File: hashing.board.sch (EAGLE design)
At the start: 136 parts, among them U1 ASIC-1, U10 EPM570GT100C5N, U2 ASIC-1, U3 ASIC-1, U4 ASIC-1, U5 ASIC-1, U6 ASIC-1, U7 ASIC-1, U8 ASIC-1, U9 AT32UC3A1256-AUT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

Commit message: before the custom cap things
before crazy edit
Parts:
- added CA1, CA2, CA3, CA4, CA5, CA6, CA7, CA8: BFL-BGA-144-SPC, casey's_custom_stuff:BFL-BGA-144-SPC
- C1, C2, C3, C4: device rcl:C-EUC0402 -> CAPACITORS:0306-REVERSE-GEO
- C5: device rcl:C-EUC0603 -> CAPACITORS:0306-REVERSE-GEO
- C6: device rcl:C-EUC0603 -> rcl:C-EUC0805
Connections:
- net GND: now also CA1.2, CA2.2, CA3.2, CA4.2, CA5.2, CA6.2, CA7.2, CA8.2
- net VDD-1VA: now also CA1.1, CA2.1, CA3.1, CA4.1
- net VDD-1VB: now also CA5.1, CA6.1, CA7.1, CA8.1

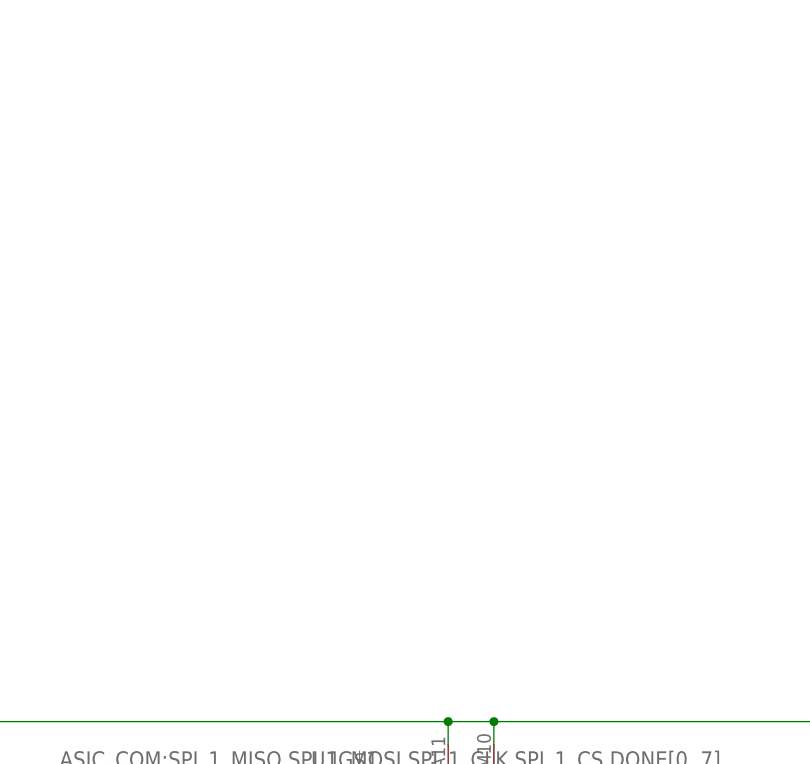
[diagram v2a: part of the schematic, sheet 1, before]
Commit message: new custom bga pkg layout
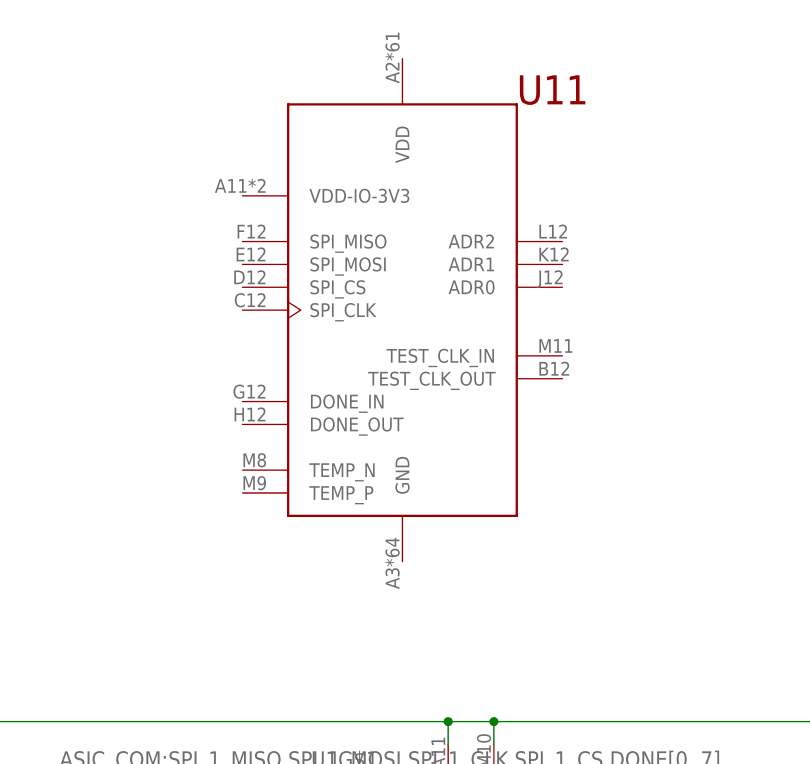
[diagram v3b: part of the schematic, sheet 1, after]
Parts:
- added U11: BFL-ASIC-1, BFL.new:BFL-ASIC-1
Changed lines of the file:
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@@
 <grid distance="0.1" unitdist="inch" unit="inch" style="lines" multiple="1" display="no" altdistance="0.01" altunitdist="inch" altunit="inch"/>
 <layers>
-<layer number="1" name="Top" color="4" fill="1" visible="yes" active="no"/>
-<layer number="2" name="Route2" color="1" fill="3" visible="yes" active="no"/>
-<layer number="3" name="Route3" color="4" fill="3" visible="yes" active="no"/>
-<layer number="14" name="Route14" color="1" fill="6" visible="yes" active="no"/>
-<layer number="15" name="Route15" color="4" fill="6" visible="yes" active="no"/>
-<layer number="16" name="Bottom" color="1" fill="1" visible="yes" active="no"/>
-<layer number="17" name="Pads" color="2" fill="1" visible="yes" active="no"/>
-<layer number="18" name="Vias" color="2" fill="1" visible="yes" active="no"/>
-<layer number="19" name="Unrouted" color="6" fill="1" visible="yes" active="no"/>
-<layer number="20" name="Dimension" color="15" fill="1" visible="yes" active="no"/>
-<layer number="21" name="tPlace" color="7" fill="1" visible="yes" active="no"/>
-<layer number="22" name="bPlace" color="7" fill="1" visible="yes" active="no"/>
-<layer number="23" name="tOrigins" color="15" fill="1" visible="yes" active="no"/>
-<layer number="24" name="bOrigins" color="15" fill="1" visible="yes" active="no"/>
-<layer number="25" name="tNames" color="7" fill="1" visible="yes" active="no"/>
-<layer number="26" name="bNames" color="7" fill="1" visible="yes" active="no"/>
-<layer number="27" name="tValues" color="7" fill="1" visible="yes" active="no"/>
-<layer number="28" name="bValues" color="7" fill="1" visible="yes" active="no"/>
+<layer number="1" name="Top" color="4" fill="1" visible="no" active="no"/>
+<layer number="2" name="Route2" color="1" fill="3" visible="no" active="no"/>
+<layer number="3" name="Route3" color="4" fill="3" visible="no" active="no"/>
+<layer number="14" name="Route14" color="1" fill="6" visible="no" active="no"/>
+<layer number="15" name="Route15" color="4" fill="6" visible="no" active="no"/>
+<layer number="16" name="Bottom" color="1" fill="1" visible="no" active="no"/>
+<layer number="17" name="Pads" color="2" fill="1" visible="no" active="no"/>
+<layer number="18" name="Vias" color="2" fill="1" visible="no" active="no"/>
+<layer number="19" name="Unrouted" color="6" fill="1" visible="no" active="no"/>
+<layer number="20" name="Dimension" color="15" fill="1" visible="no" active="no"/>
+<layer number="21" name="tPlace" color="7" fill="1" visible="no" active="no"/>
+<layer number="22" name="bPlace" color="7" fill="1" visible="no" active="no"/>
+<layer number="23" name="tOrigins" color="15" fill="1" visible="no" active="no"/>
+<layer number="24" name="bOrigins" color="15" fill="1" visible="no" active="no"/>
+<layer number="25" name="tNames" color="7" fill="1" visible="no" active="no"/>
+<layer number="26" name="bNames" color="7" fill="1" visible="no" active="no"/>
+<layer number="27" name="tValues" color="7" fill="1" visible="no" active="no"/>
+<layer number="28" name="bValues" color="7" fill="1" visible="no" active="no"/>
 <layer number="29" name="tStop" color="7" fill="3" visible="no" active="no"/>
 <layer number="30" name="bStop" color="7" fill="6" visible="no" active="no"/>
@@
 <layer number="35" name="tGlue" color="7" fill="4" visible="no" active="no"/>
 <layer number="36" name="bGlue" color="7" fill="5" visible="no" active="no"/>
-<layer number="37" name="tTest" color="7" fill="1" visible="yes" active="no"/>
-<layer number="38" name="bTest" color="7" fill="1" visible="yes" active="no"/>
+<layer number="37" name="tTest" color="7" fill="1" visible="no" active="no"/>
+<layer number="38" name="bTest" color="7" fill="1" visible="no" active="no"/>
 <layer number="39" name="tKeepout" color="4" fill="11" visible="no" active="no"/>
 <layer number="40" name="bKeepout" color="1" fill="11" visible="no" active="no"/>
@@
 <layer number="44" name="Drills" color="7" fill="1" visible="no" active="no"/>
 <layer number="45" name="Holes" color="7" fill="1" visible="no" active="no"/>
-<layer number="46" name="Milling" color="3" fill="1" visible="yes" active="no"/>
-<layer number="47" name="Measures" color="7" fill="1" visible="yes" active="no"/>
-<layer number="48" name="Document" color="7" fill="1" visible="yes" active="no"/>
-<layer number="49" name="Reference" color="7" fill="1" visible="yes" active="no"/>
-<layer number="51" name="tDocu" color="7" fill="1" visible="yes" active="no"/>
-<layer number="52" name="bDocu" color="7" fill="1" visible="yes" active="no"/>
+<layer number="46" name="Milling" color="3" fill="1" visible="no" active="no"/>
+<layer number="47" name="Measures" color="7" fill="1" visible="no" active="no"/>
+<layer number="48" name="Document" color="7" fill="1" visible="no" active="no"/>
+<layer number="49" name="Reference" color="7" fill="1" visible="no" active="no"/>
+<layer number="51" name="tDocu" color="7" fill="1" visible="no" active="no"/>
+<layer number="52" name="bDocu" color="7" fill="1" visible="no" active="no"/>
 <layer number="91" name="Nets" color="2" fill="1" visible="yes" active="yes"/>
 <layer number="92" name="Busses" color="1" fill="1" visible="yes" active="yes"/>
@@
 <part name="CA7" library="casey's_custom_stuff" deviceset="BFL-BGA-144-SPC" device=""/>
 <part name="CA8" library="casey's_custom_stuff" deviceset="BFL-BGA-144-SPC" device=""/>
+<part name="U11" library="BFL.new" deviceset="BFL-ASIC-1" device=""/>
 </parts>
 <sheets>
@@
 <instance part="FRAME2" gate="G$1" x="0" y="0"/>
 <instance part="FRAME2" gate="G$2" x="325.12" y="0"/>
+<instance part="U11" gate="G$1" x="139.7" y="213.36"/>
 </instances>
 <busses>

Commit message: broken
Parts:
- removed U11: BFL-ASIC-1, BFL.new:BFL-ASIC-1
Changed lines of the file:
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@@
 <grid distance="0.1" unitdist="inch" unit="inch" style="lines" multiple="1" display="no" altdistance="0.01" altunitdist="inch" altunit="inch"/>
 <layers>
-<layer number="1" name="Top" color="4" fill="1" visible="no" active="no"/>
-<layer number="2" name="Route2" color="1" fill="3" visible="no" active="no"/>
-<layer number="3" name="Route3" color="4" fill="3" visible="no" active="no"/>
-<layer number="14" name="Route14" color="1" fill="6" visible="no" active="no"/>
-<layer number="15" name="Route15" color="4" fill="6" visible="no" active="no"/>
-<layer number="16" name="Bottom" color="1" fill="1" visible="no" active="no"/>
-<layer number="17" name="Pads" color="2" fill="1" visible="no" active="no"/>
-<layer number="18" name="Vias" color="2" fill="1" visible="no" active="no"/>
-<layer number="19" name="Unrouted" color="6" fill="1" visible="no" active="no"/>
-<layer number="20" name="Dimension" color="15" fill="1" visible="no" active="no"/>
-<layer number="21" name="tPlace" color="7" fill="1" visible="no" active="no"/>
-<layer number="22" name="bPlace" color="7" fill="1" visible="no" active="no"/>
-<layer number="23" name="tOrigins" color="15" fill="1" visible="no" active="no"/>
-<layer number="24" name="bOrigins" color="15" fill="1" visible="no" active="no"/>
-<layer number="25" name="tNames" color="7" fill="1" visible="no" active="no"/>
-<layer number="26" name="bNames" color="7" fill="1" visible="no" active="no"/>
-<layer number="27" name="tValues" color="7" fill="1" visible="no" active="no"/>
-<layer number="28" name="bValues" color="7" fill="1" visible="no" active="no"/>
+<layer number="1" name="Top" color="4" fill="1" visible="yes" active="no"/>
+<layer number="2" name="Route2" color="1" fill="3" visible="yes" active="no"/>
+<layer number="3" name="Route3" color="4" fill="3" visible="yes" active="no"/>
+<layer number="14" name="Route14" color="1" fill="6" visible="yes" active="no"/>
+<layer number="15" name="Route15" color="4" fill="6" visible="yes" active="no"/>
+<layer number="16" name="Bottom" color="1" fill="1" visible="yes" active="no"/>
+<layer number="17" name="Pads" color="2" fill="1" visible="yes" active="no"/>
+<layer number="18" name="Vias" color="2" fill="1" visible="yes" active="no"/>
+<layer number="19" name="Unrouted" color="6" fill="1" visible="yes" active="no"/>
+<layer number="20" name="Dimension" color="15" fill="1" visible="yes" active="no"/>
+<layer number="21" name="tPlace" color="7" fill="1" visible="yes" active="no"/>
+<layer number="22" name="bPlace" color="7" fill="1" visible="yes" active="no"/>
+<layer number="23" name="tOrigins" color="15" fill="1" visible="yes" active="no"/>
+<layer number="24" name="bOrigins" color="15" fill="1" visible="yes" active="no"/>
+<layer number="25" name="tNames" color="7" fill="1" visible="yes" active="no"/>
+<layer number="26" name="bNames" color="7" fill="1" visible="yes" active="no"/>
+<layer number="27" name="tValues" color="7" fill="1" visible="yes" active="no"/>
+<layer number="28" name="bValues" color="7" fill="1" visible="yes" active="no"/>
 <layer number="29" name="tStop" color="7" fill="3" visible="no" active="no"/>
 <layer number="30" name="bStop" color="7" fill="6" visible="no" active="no"/>
@@
 <layer number="35" name="tGlue" color="7" fill="4" visible="no" active="no"/>
 <layer number="36" name="bGlue" color="7" fill="5" visible="no" active="no"/>
-<layer number="37" name="tTest" color="7" fill="1" visible="no" active="no"/>
-<layer number="38" name="bTest" color="7" fill="1" visible="no" active="no"/>
+<layer number="37" name="tTest" color="7" fill="1" visible="yes" active="no"/>
+<layer number="38" name="bTest" color="7" fill="1" visible="yes" active="no"/>
 <layer number="39" name="tKeepout" color="4" fill="11" visible="no" active="no"/>
 <layer number="40" name="bKeepout" color="1" fill="11" visible="no" active="no"/>
@@
 <layer number="44" name="Drills" color="7" fill="1" visible="no" active="no"/>
 <layer number="45" name="Holes" color="7" fill="1" visible="no" active="no"/>
-<layer number="46" name="Milling" color="3" fill="1" visible="no" active="no"/>
-<layer number="47" name="Measures" color="7" fill="1" visible="no" active="no"/>
-<layer number="48" name="Document" color="7" fill="1" visible="no" active="no"/>
-<layer number="49" name="Reference" color="7" fill="1" visible="no" active="no"/>
-<layer number="51" name="tDocu" color="7" fill="1" visible="no" active="no"/>
-<layer number="52" name="bDocu" color="7" fill="1" visible="no" active="no"/>
+<layer number="46" name="Milling" color="3" fill="1" visible="yes" active="no"/>
+<layer number="47" name="Measures" color="7" fill="1" visible="yes" active="no"/>
+<layer number="48" name="Document" color="7" fill="1" visible="yes" active="no"/>
+<layer number="49" name="Reference" color="7" fill="1" visible="yes" active="no"/>
+<layer number="51" name="tDocu" color="7" fill="1" visible="yes" active="no"/>
+<layer number="52" name="bDocu" color="7" fill="1" visible="yes" active="no"/>
 <layer number="91" name="Nets" color="2" fill="1" visible="yes" active="yes"/>
 <layer number="92" name="Busses" color="1" fill="1" visible="yes" active="yes"/>
@@
 <part name="CA7" library="casey's_custom_stuff" deviceset="BFL-BGA-144-SPC" device=""/>
 <part name="CA8" library="casey's_custom_stuff" deviceset="BFL-BGA-144-SPC" device=""/>
-<part name="U11" library="BFL.new" deviceset="BFL-ASIC-1" device=""/>
 </parts>
 <sheets>
@@
 <instance part="FRAME2" gate="G$1" x="0" y="0"/>
 <instance part="FRAME2" gate="G$2" x="325.12" y="0"/>
-<instance part="U11" gate="G$1" x="139.7" y="213.36"/>
 </instances>
 <busses>
